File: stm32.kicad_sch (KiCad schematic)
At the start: 29 parts, among them J13 Screw_Terminal_01x04, U22 REF3030, U23 STM32H743VITx, Y4 8Mhz

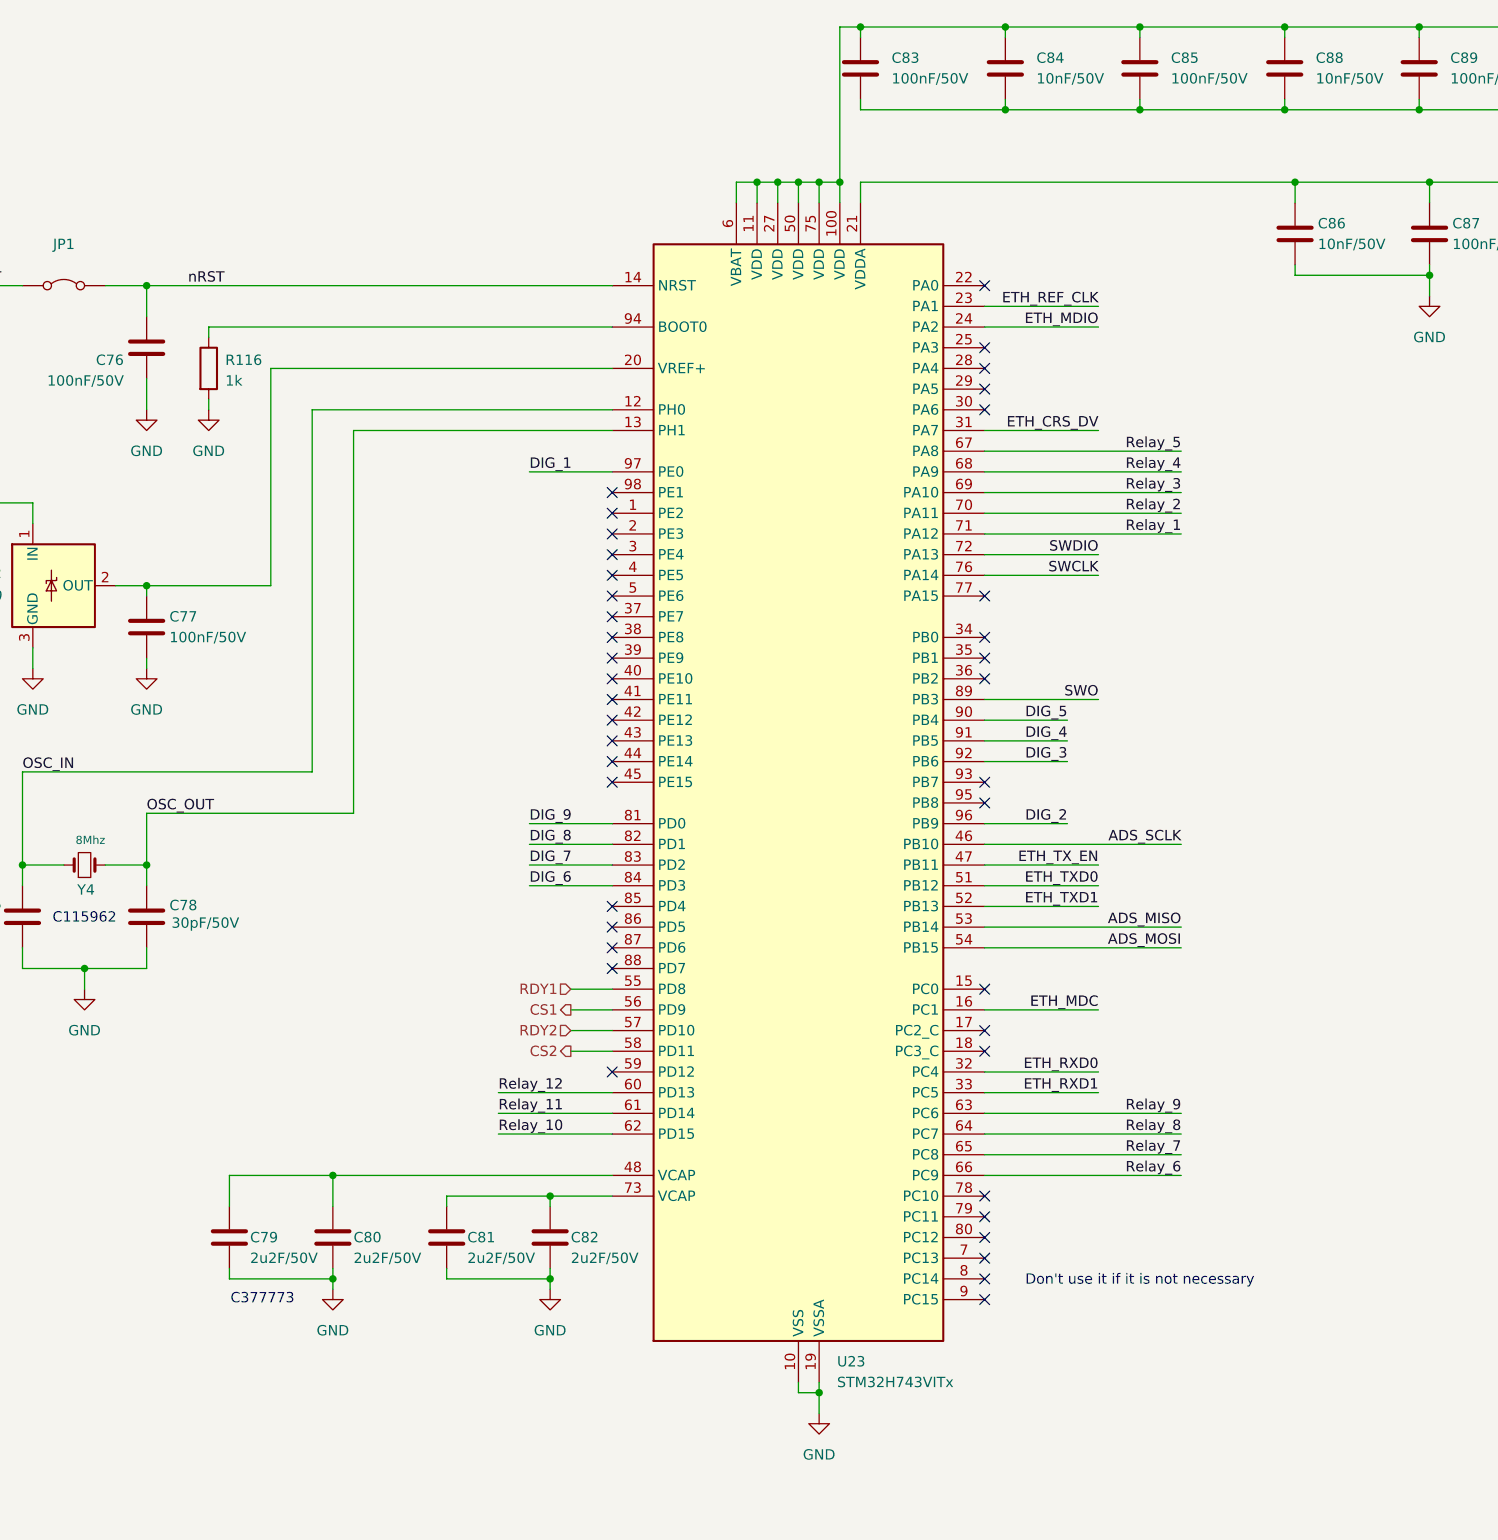
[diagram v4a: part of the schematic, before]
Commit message: Se crea nueva version debido a que el anterior diseño estaba para un uC stm32h7. Este nuevo diseño corresponde al stm32f407v utilizado en el esterilizador y otros proyectos conocidos en la empresa.
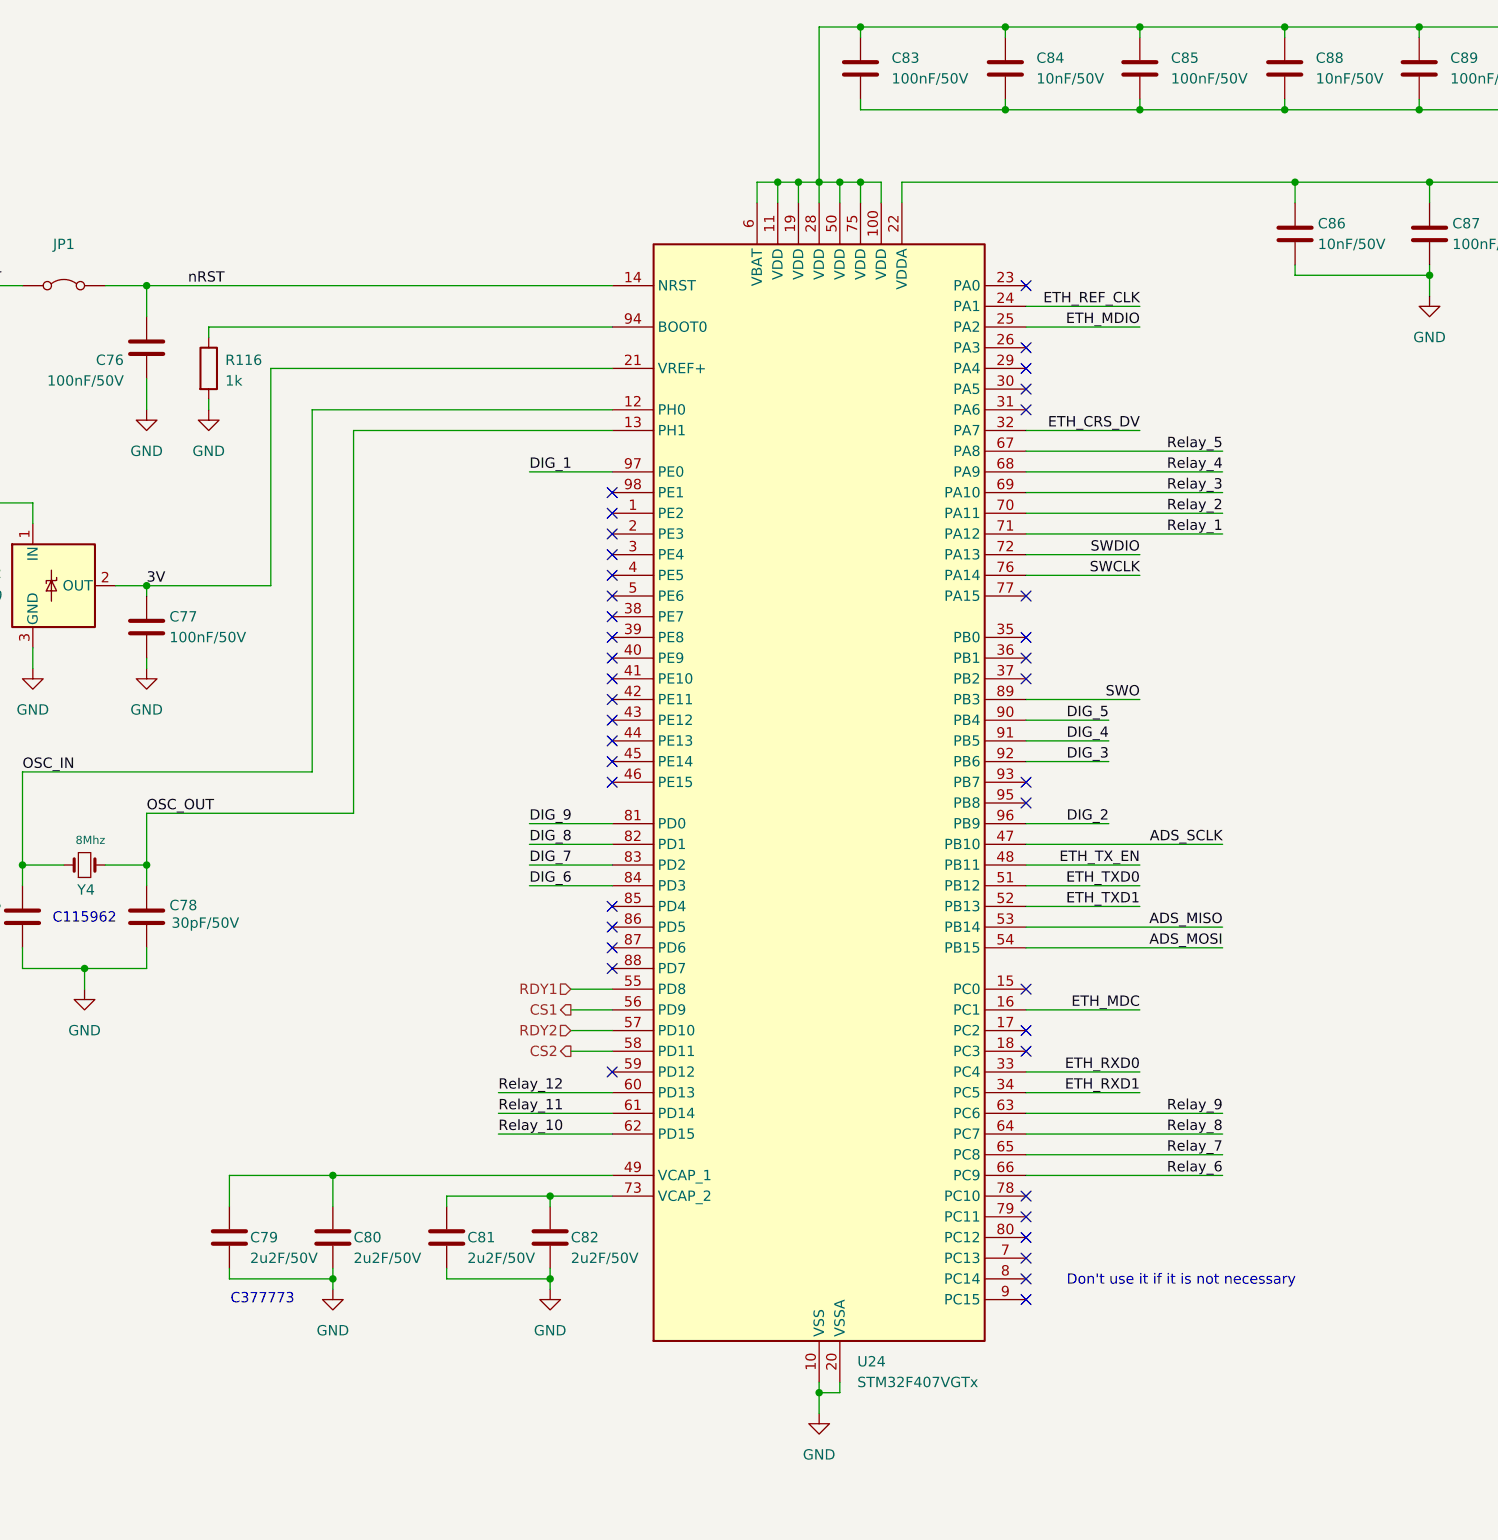
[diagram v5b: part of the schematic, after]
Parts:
- removed U23: STM32H743VITx, Package_QFP:LQFP-100_14x14mm_P0.5mm, symbol MCU_ST_STM32H7:STM32H743VITx
- added U24: STM32F407VGTx, Package_QFP:LQFP-100_14x14mm_P0.5mm, symbol MCU_ST_STM32F4:STM32F407VGTx
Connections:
- net ADS_MISO: now also U24.53 (PB14)
- net ADS_MOSI: now also U24.54 (PB15)
- net ADS_SCLK: now also U24.47 (PB10)
- net CS1: now also U24.56 (PD9)
- net CS2: now also U24.58 (PD11)
- net DIG_1: now also U24.97 (PE0)
- net DIG_2: now also U24.96 (PB9)
- net DIG_3: now also U24.92 (PB6)
- net DIG_4: now also U24.91 (PB5)
- net DIG_5: now also U24.90 (PB4)
- net DIG_6: now also U24.84 (PD3)
- net DIG_7: now also U24.83 (PD2)
- net DIG_8: now also U24.82 (PD1)
- net DIG_9: now also U24.81 (PD0)
- net ETH_CRS_DV: now also U24.32 (PA7)
- net ETH_MDC: now also U24.16 (PC1)
- net ETH_MDIO: now also U24.25 (PA2)
- net ETH_REF_CLK: now also U24.24 (PA1)
- net ETH_RXD0: now also U24.33 (PC4)
- net ETH_RXD1: now also U24.34 (PC5)
- net ETH_TXD0: now also U24.51 (PB12)
- net ETH_TXD1: now also U24.52 (PB13)
- net ETH_TX_EN: now also U24.48 (PB11)
- net GND: now also U24.10 (VSS), U24.20 (VSSA), U24.27 (VSS), U24.74 (VSS), U24.99 (VSS)
- net OSC_IN: now also U24.12 (PH0)
- net OSC_OUT: now also U24.13 (PH1)
- net RDY1: now also U24.55 (PD8)
- net RDY2: now also U24.57 (PD10)
- net Relay_1: now also U24.71 (PA12)
- net Relay_10: now also U24.62 (PD15)
- net Relay_11: now also U24.61 (PD14)
- net Relay_12: now also U24.60 (PD13)
- net Relay_2: now also U24.70 (PA11)
- net Relay_3: now also U24.69 (PA10)
- net Relay_4: now also U24.68 (PA9)
- net Relay_5: now also U24.67 (PA8)
- net Relay_6: now also U24.66 (PC9)
- net Relay_7: now also U24.65 (PC8)
- net Relay_8: now also U24.64 (PC7)
- net Relay_9: now also U24.63 (PC6)
- net SWCLK: now also U24.76 (PA14)
- net SWDIO: now also U24.72 (PA13)
- net SWO: now also U24.89 (PB3)
- net VDD_3V3: now also U24.100 (VDD), U24.11 (VDD), U24.19 (VDD), U24.28 (VDD), U24.50 (VDD), U24.6 (VBAT), U24.75 (VDD)
- net nRST: now also U24.14 (NRST)
- net at C81.1, C82.1: now also U24.73 (VCAP_2)
- net at C86.1, C87.1, FB2.1: now also U24.22 (VDDA)
- net at C79.1, C80.1: now also U24.49 (VCAP_1)
- net at R116.1: now also U24.94 (BOOT0)
- net 3V: now reaches C77.1, U22.2 (OUT)
- net 3V: now also U24.21 (VREF+)

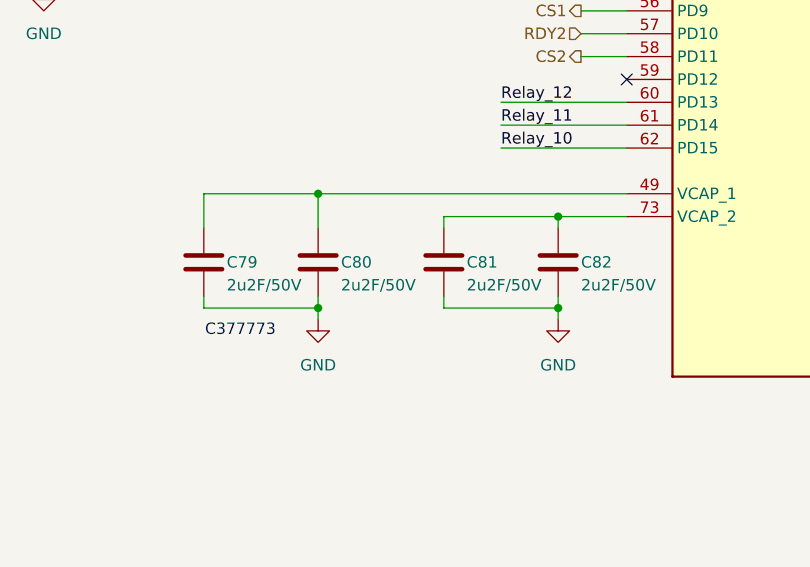
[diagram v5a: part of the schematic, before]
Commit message: Se corrige el nombre para la ref de 2.5V para los canales análogos, Se corrigen quita un capacitor en cada pin VCAP, Se actualiza PCB
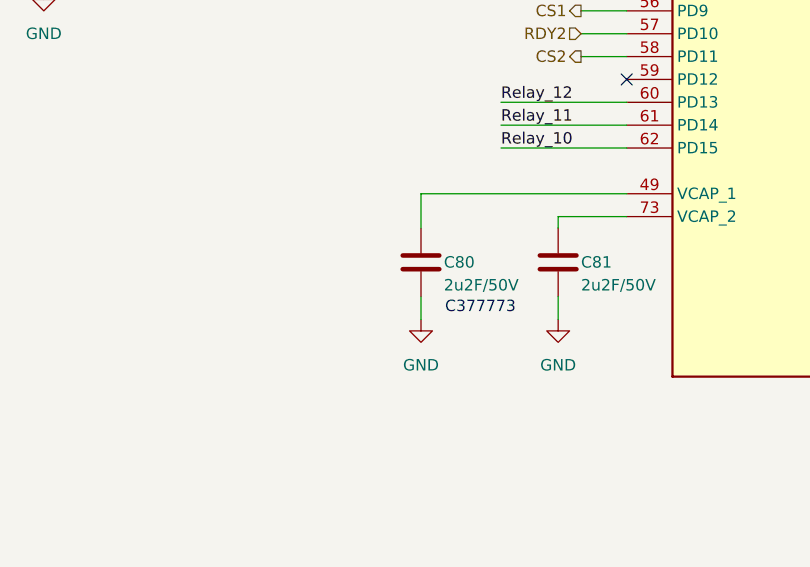
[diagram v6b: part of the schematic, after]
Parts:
- removed C79, C82: 2u2F/50V, Capacitor_SMD:C_0805_2012Metric, symbol 1-Capacitor:C_0805
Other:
- moved on the sheet: C80, C81

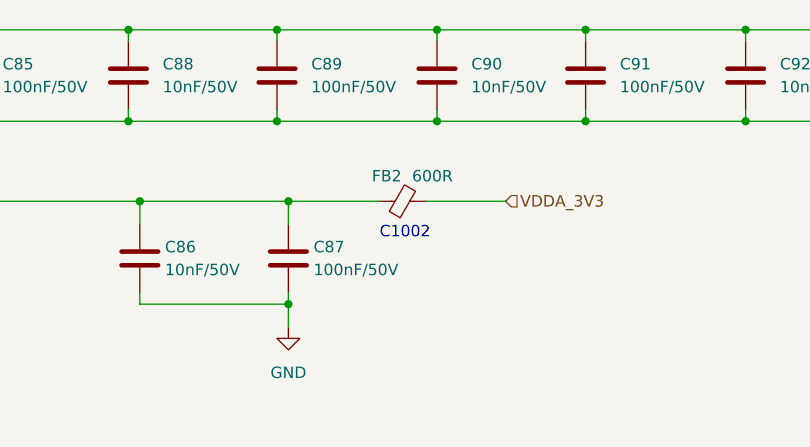
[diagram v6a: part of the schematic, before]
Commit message: Se añaden leds a la entrada de los Namur. Se estandariza y revisan varios footprints de los capacitores. El cambio no fue demasiado, se corrigio en placa. Se hacen algunos cambios adicionales a los valores. Se realiza un avance para jlcpcb
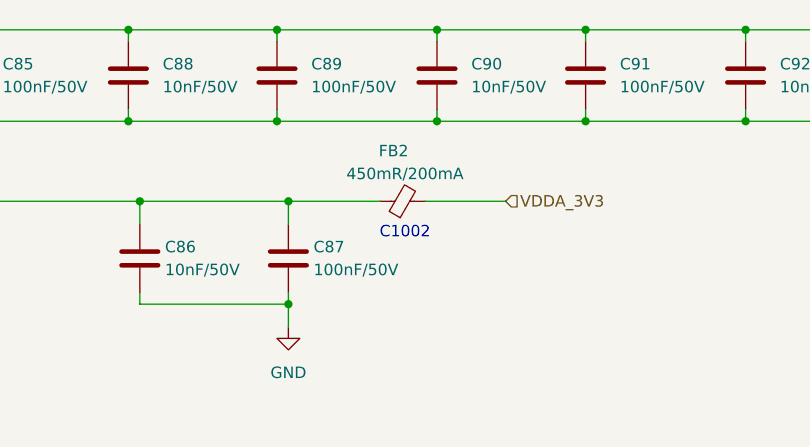
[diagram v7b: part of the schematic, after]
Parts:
- FB2: value 600R -> 450mR/200mA; footprint Inductor_SMD:L_0805_2012Metric -> Inductor_SMD:L_0603_1608Metric
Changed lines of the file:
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@@
 		(dnp no)
 		(property "Reference" "FB2"
-			(at 294.132 39.116 90)
+			(at 294.894 36.322 90)
 			(effects
 				(font
@@
 			)
 		)
-		(property "Value" "600R"
-			(at 299.212 39.116 90)
+		(property "Value" "450mR/200mA"
+			(at 296.164 38.862 90)
 			(effects
 				(font
@@
 			)
 		)
-		(property "Footprint" "Inductor_SMD:L_0805_2012Metric"
+		(property "Footprint" "Inductor_SMD:L_0603_1608Metric"
 			(at 295.91 43.688 90)
 			(effects
